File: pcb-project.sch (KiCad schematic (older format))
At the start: 146 parts, among them SW1 SW_PUSH, U2 ATMEGA32U4, X2 XTAL_GND

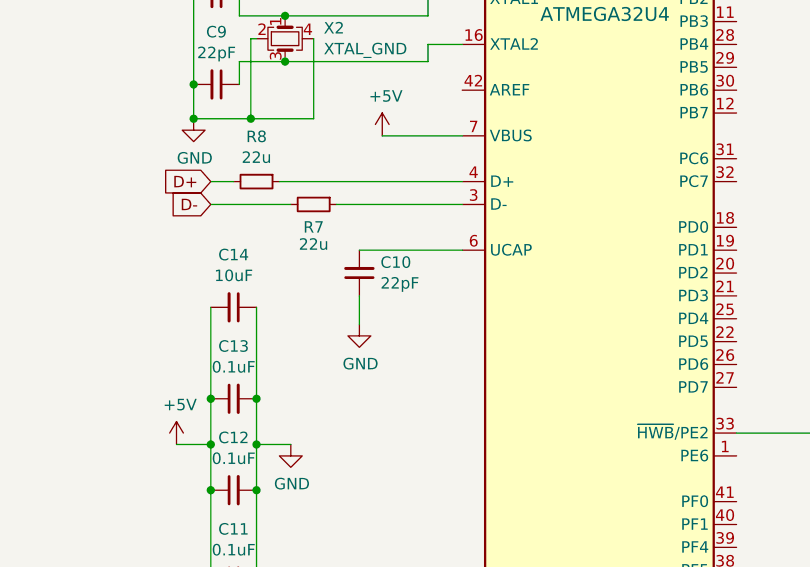
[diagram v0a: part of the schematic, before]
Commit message: Added Traces
No idea if they're entirely correct, hopefully can check it all out for myself and maybe have someone on Geekhack review it.
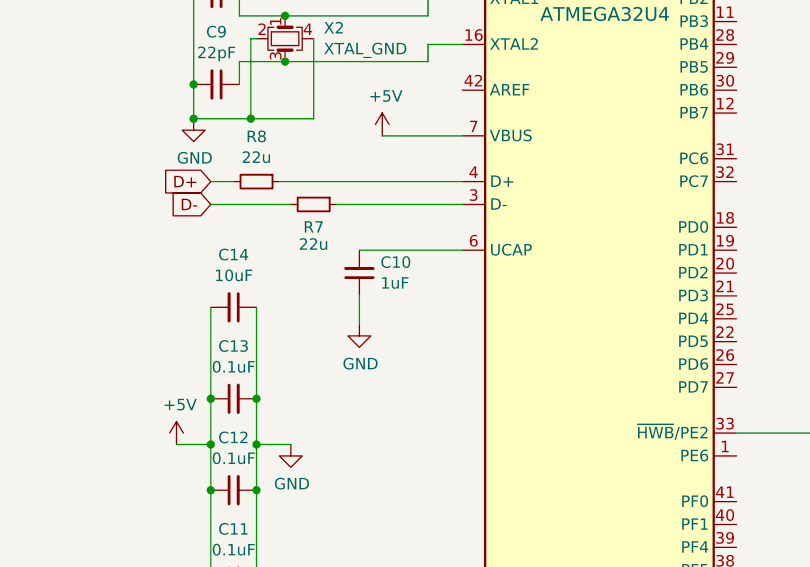
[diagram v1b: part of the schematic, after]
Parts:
- C10: value 22pF -> 1uF
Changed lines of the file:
@@
 P 18775 4450
 F 0 "C10" H 18683 4404 50  0000 R CNN
-F 1 "22pF" H 18683 4495 50  0000 R CNN
+F 1 "1uF" H 18683 4495 50  0000 R CNN
 F 2 "Capacitor_SMD:C_0805_2012Metric" H 18775 4450 50  0001 C CNN
 F 3 "~" H 18775 4450 50  0001 C CNN

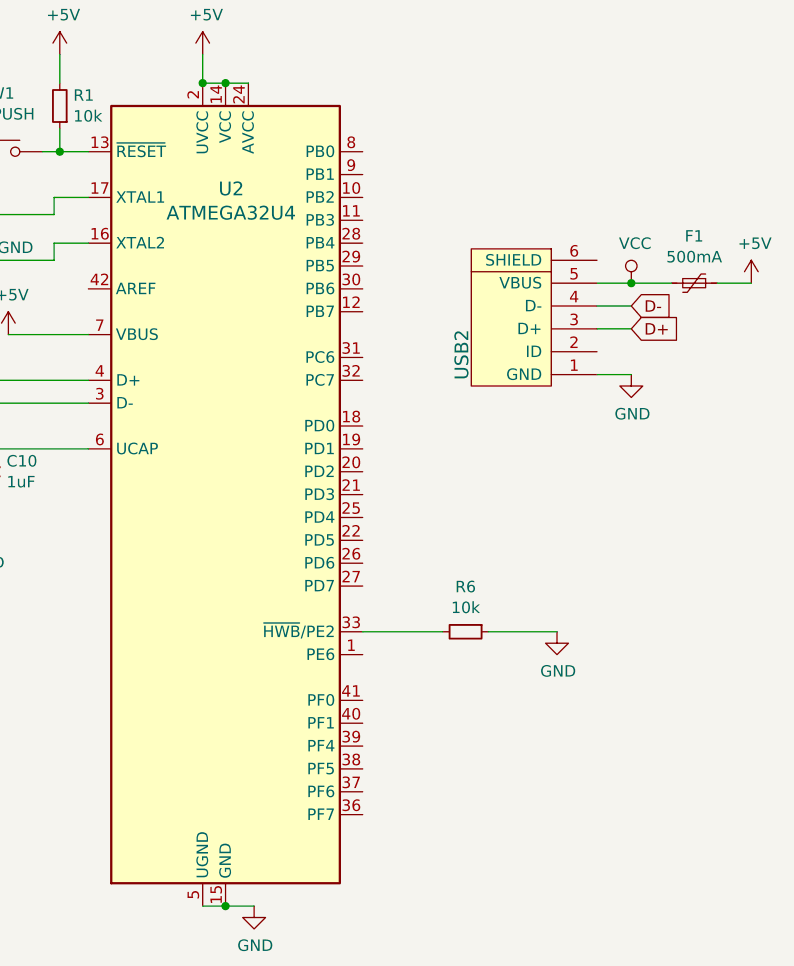
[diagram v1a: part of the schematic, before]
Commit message: Missing Matrix Connections
The schematic and net list have been updated but this is prior to the pcb recieving the updated net list.
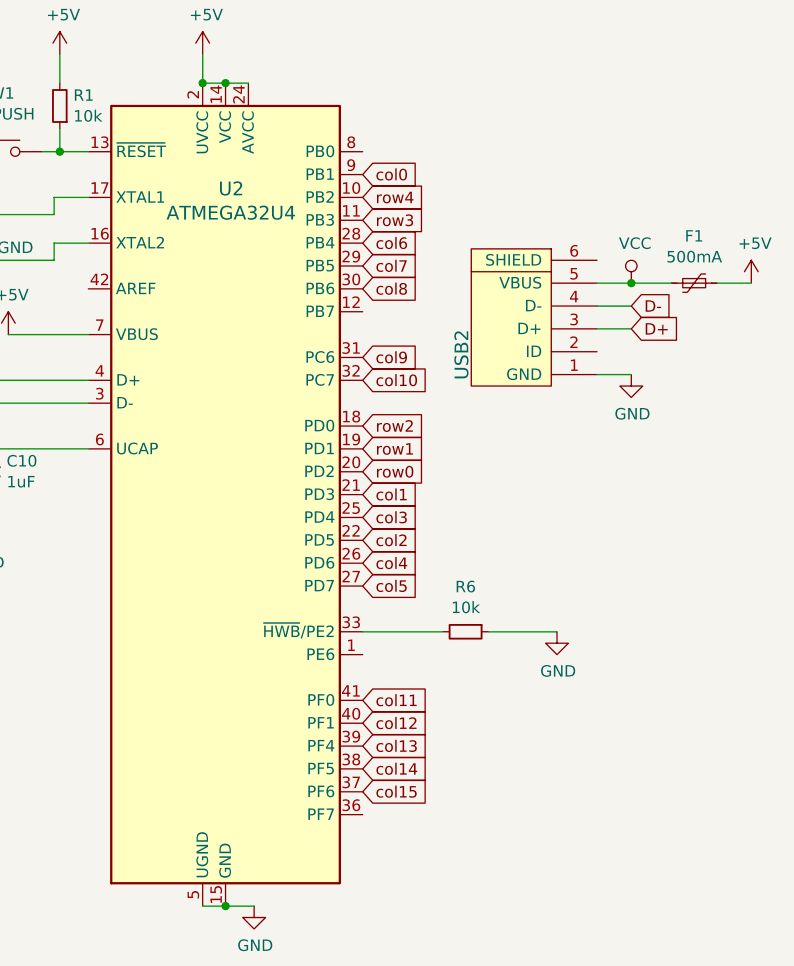
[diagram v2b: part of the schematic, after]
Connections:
- net col0: now also U2.9 (PB1)
- net col1: now also U2.21 (PD3)
- net col10: now also U2.32 (PC7)
- net col11: now also U2.41 (PF0)
- net col12: now also U2.40 (PF1)
- net col13: now also U2.39 (PF4)
- net col14: now also U2.38 (PF5)
- net col15: now also U2.37 (PF6)
- net col2: now also U2.22 (PD5)
- net col3: now also U2.25 (PD4)
- net col4: now also U2.26 (PD6)
- net col5: now also U2.27 (PD7)
- net col6: now also U2.28 (PB4)
- net col7: now also U2.29 (PB5)
- net col8: now also U2.30 (PB6)
- net col9: now also U2.31 (PC6)
- net row0: now also U2.20 (PD2)
- net row1: now also U2.19 (PD1)
- net row2: now also U2.18 (PD0)
- net row3: now also U2.11 (PB3)
- net row4: now also U2.10 (PB2)
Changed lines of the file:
@@
 EESchema Schematic File Version 4
+LIBS:pcb-project-cache
 EELAYER 29 0
 EELAYER END
@@
 	19075 3450 19225 3450
 Connection ~ 18450 3525
+Text GLabel 20425 3150 2    50   Input ~ 0
+col0
+Text GLabel 20425 4450 2    50   Input ~ 0
+row0
+Text GLabel 20425 4350 2    50   Input ~ 0
+row1
+Text GLabel 20425 4250 2    50   Input ~ 0
+row2
+Text GLabel 20425 3350 2    50   Input ~ 0
+row3
+Text GLabel 20425 3250 2    50   Input ~ 0
+row4
+Text GLabel 20425 4550 2    50   Input ~ 0
+col1
+Text GLabel 20425 4750 2    50   Input ~ 0
+col2
+Text GLabel 20425 4650 2    50   Input ~ 0
+col3
+Text GLabel 20425 4850 2    50   Input ~ 0
+col4
+Text GLabel 20425 4950 2    50   Input ~ 0
+col5
+Text GLabel 20425 3450 2    50   Input ~ 0
+col6
+Text GLabel 20425 3550 2    50   Input ~ 0
+col7
+Text GLabel 20425 3650 2    50   Input ~ 0
+col8
+Text GLabel 20425 3950 2    50   Input ~ 0
+col9
+Text GLabel 20425 4050 2    50   Input ~ 0
+col10
+Text GLabel 20425 5450 2    50   Input ~ 0
+col11
+Text GLabel 20425 5550 2    50   Input ~ 0
+col12
+Text GLabel 20425 5650 2    50   Input ~ 0
+col13
+Text GLabel 20425 5750 2    50   Input ~ 0
+col14
+Text GLabel 20425 5850 2    50   Input ~ 0
+col15
 $EndSCHEMATC

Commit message: "Completed" PCB and Bongocat
The PCB is basically done. Just wanted to add a decorative bongocat for a logo and then get the files that are actually used for production ready to go.
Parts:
- SW1: footprint Button_Switch_SMD:SW_SPST_TL3342 -> random-keyboard-parts:SKQG-1155865
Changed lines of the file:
@@
 F 0 "SW1" H 18825 3305 50  0000 C CNN
 F 1 "SW_PUSH" H 18825 3214 50  0000 C CNN
-F 2 "Button_Switch_SMD:SW_SPST_TL3342" H 18825 3050 60  0001 C CNN
+F 2 "random-keyboard-parts:SKQG-1155865" H 18825 3050 60  0001 C CNN
 F 3 "" H 18825 3050 60  0000 C CNN
 	1    18825 3050

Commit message: Changed the Crystal to a different footprint
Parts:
- X2: footprint Crystal:Crystal_SMD_5032-4Pin_5.0x3.2mm -> Crystal:Crystal_SMD_3225-4Pin_3.2x2.5mm
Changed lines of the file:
@@
 F 0 "X2" V 18404 3594 50  0000 L CNN
 F 1 "XTAL_GND" V 18495 3594 50  0000 L CNN
-F 2 "Crystal:Crystal_SMD_5032-4Pin_5.0x3.2mm" V 18541 3594 50  0001 L CNN
+F 2 "Crystal:Crystal_SMD_3225-4Pin_3.2x2.5mm" V 18541 3594 50  0001 L CNN
 F 3 "~" H 18450 3425 50  0001 C CNN
 	1    18450 3425

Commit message: Latest Version of the PCB
Had to modify the bottom row to use the proper 7u Spacebar and 1.5u Alts. Same as many uniform HHKB layout boards.
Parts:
- K_ALT1, K_ALT2: footprint MX_Alps_Hybrid:MX-1.25U-NoLED -> MX_Alps_Hybrid:MX-1.5U-NoLED
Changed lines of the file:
@@
 F 0 "K_ALT2" H 4725 6058 60  0000 C CNN
 F 1 "KEYSW" H 4725 5725 60  0001 C CNN
-F 2 "MX_Alps_Hybrid:MX-1.25U-NoLED" H 4725 5825 60  0001 C CNN
+F 2 "MX_Alps_Hybrid:MX-1.5U-NoLED" H 4725 5825 60  0001 C CNN
 F 3 "" H 4725 5825 60  0000 C CNN
 	1    4725 5825
@@
 F 0 "K_ALT1" H 6725 6058 60  0000 C CNN
 F 1 "KEYSW" H 6725 5725 60  0001 C CNN
-F 2 "MX_Alps_Hybrid:MX-1.25U-NoLED" H 6725 5825 60  0001 C CNN
+F 2 "MX_Alps_Hybrid:MX-1.5U-NoLED" H 6725 5825 60  0001 C CNN
 F 3 "" H 6725 5825 60  0000 C CNN
 	1    6725 5825

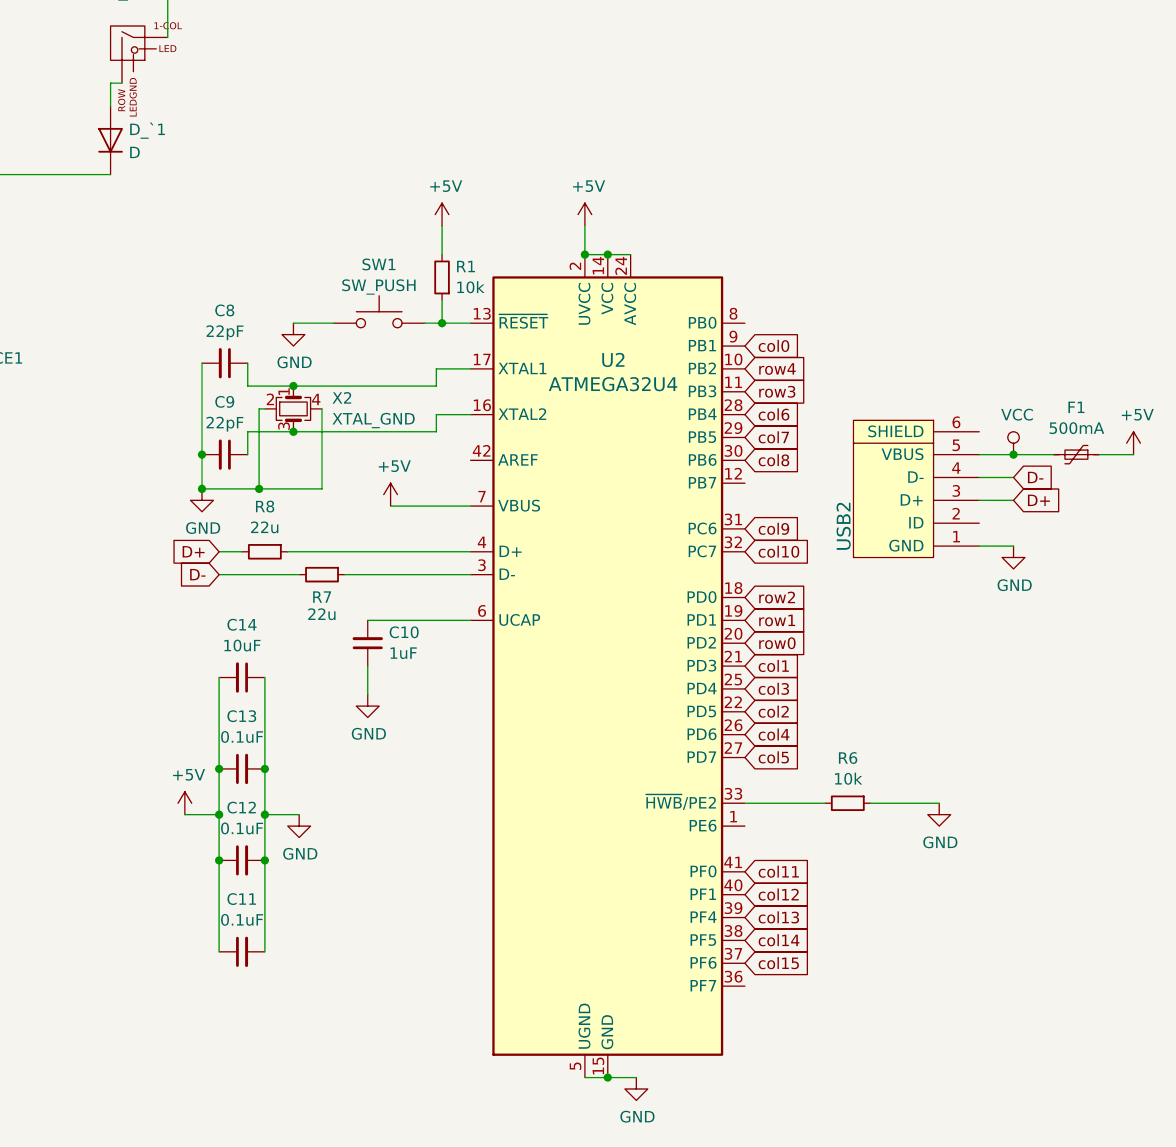
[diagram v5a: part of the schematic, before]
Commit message: Teensy Version of the PCB Project
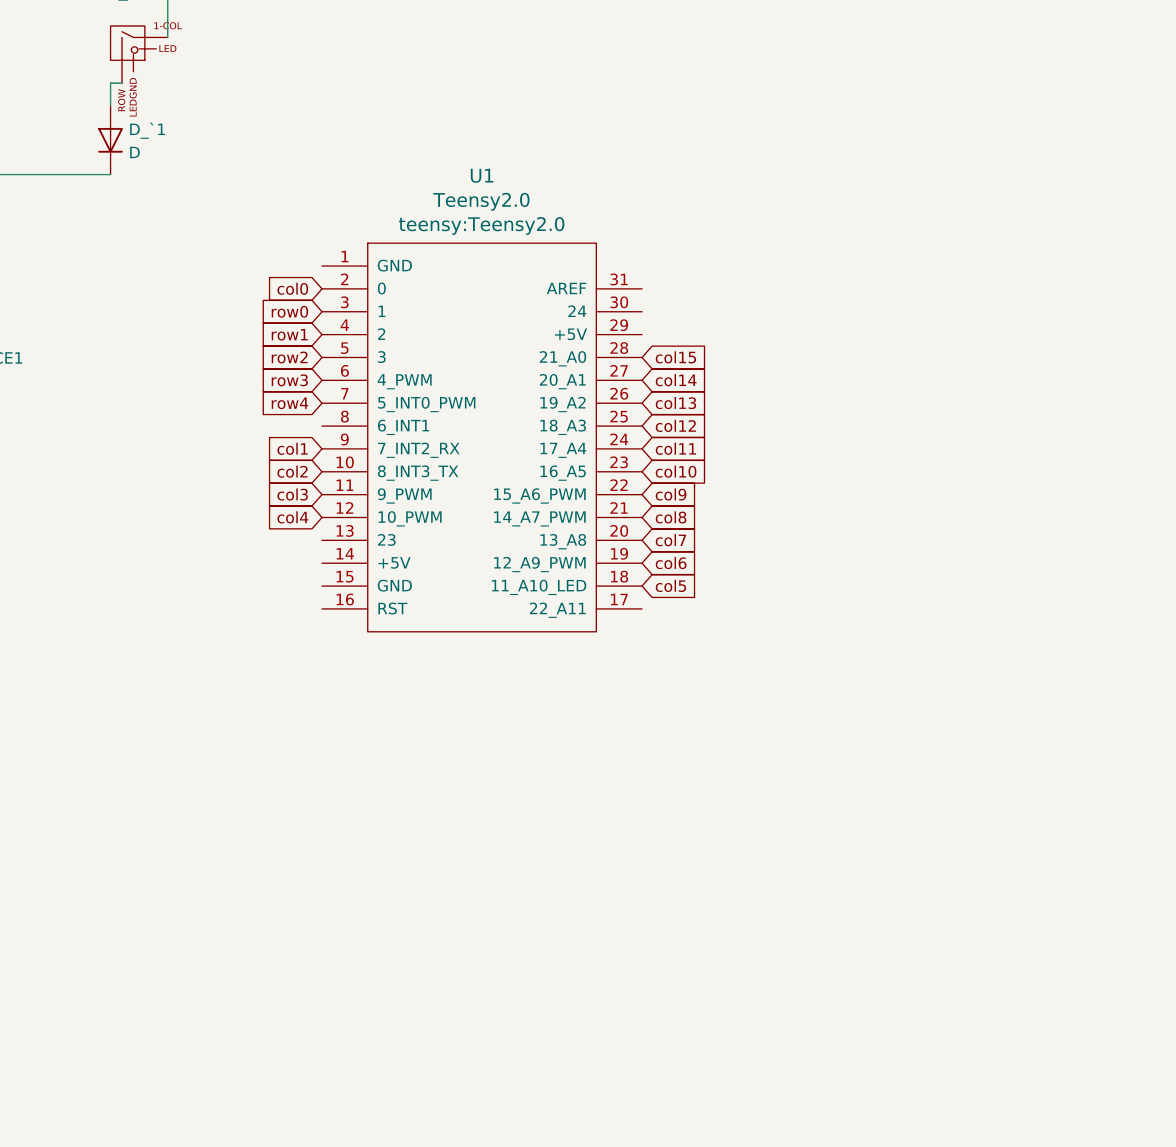
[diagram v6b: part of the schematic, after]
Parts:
- removed C10: 1uF, Capacitor_SMD:C_0805_2012Metric, symbol Device:C_Small
- removed C11, C12, C13: 0.1uF, Capacitor_SMD:C_0805_2012Metric, symbol Device:C_Small
- removed C14: 10uF, Capacitor_SMD:C_0805_2012Metric, symbol Device:C_Small
- removed C8, C9: 22pF, Capacitor_SMD:C_0805_2012Metric, symbol Device:C_Small
- removed F1: 500mA, Fuse:Fuse_1206_3216Metric, symbol Device:Polyfuse_Small
- removed R1, R6: 10k, Resistor_SMD:R_0805_2012Metric, symbol Device:R_Small
- removed R7, R8: 22u, Resistor_SMD:R_0805_2012Metric, symbol Device:R_Small
- removed SW1: SW_PUSH, random-keyboard-parts:SKQG-1155865, symbol Switch:SW_Push
- removed U2: ATMEGA32U4, Package_QFP:TQFP-44_10x10mm_P0.8mm, symbol MCU_Microchip_ATmega:ATmega32U4-AU
- removed USB2: USB_mini_micro_B, random-keyboard-parts:Molex-0548190589, symbol random-keyboard-parts:Molex-0548190589
- removed X2: XTAL_GND, Crystal:Crystal_SMD_3225-4Pin_3.2x2.5mm, symbol Device:Crystal_GND24_Small
- added U1: Teensy2.0, teensy:Teensy2.0, symbol teensy:Teensy2.0
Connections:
- net col0: now also U1.2 (0)
- net col1: now also U1.9 (7_INT2_RX)
- net col10: now also U1.23 (16_A5)
- net col11: now also U1.24 (17_A4)
- net col12: now also U1.25 (18_A3)
- net col13: now also U1.26 (19_A2)
- net col14: now also U1.27 (20_A1)
- net col15: now also U1.28 (21_A0)
- net col2: now also U1.10 (8_INT3_TX)
- net col3: now also U1.11 (9_PWM)
- net col4: now also U1.12 (10_PWM)
- net col5: now also U1.18 (11_A10_LED)
- net col6: now also U1.19 (12_A9_PWM)
- net col7: now also U1.20 (13_A8)
- net col8: now also U1.21 (14_A7_PWM)
- net col9: now also U1.22 (15_A6_PWM)
- net row0: now also U1.3 (1)
- net row1: now also U1.4 (2)
- net row2: now also U1.5 (3)
- net row3: now also U1.6 (4_PWM)
- net row4: now also U1.7 (5_INT0_PWM)
